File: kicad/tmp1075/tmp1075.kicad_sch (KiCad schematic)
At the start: 17 parts, among them J1 Conn_01x05, J2 Conn_01x05, U1 TMP1075DSG

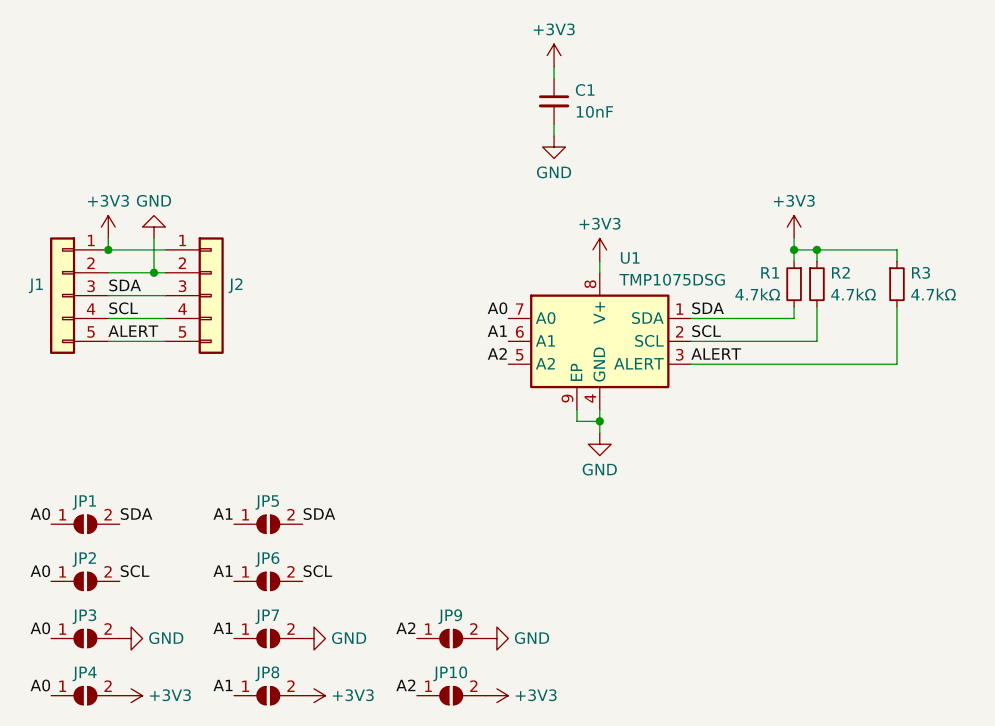
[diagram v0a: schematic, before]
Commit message: take 2 on tmp1075 breakout
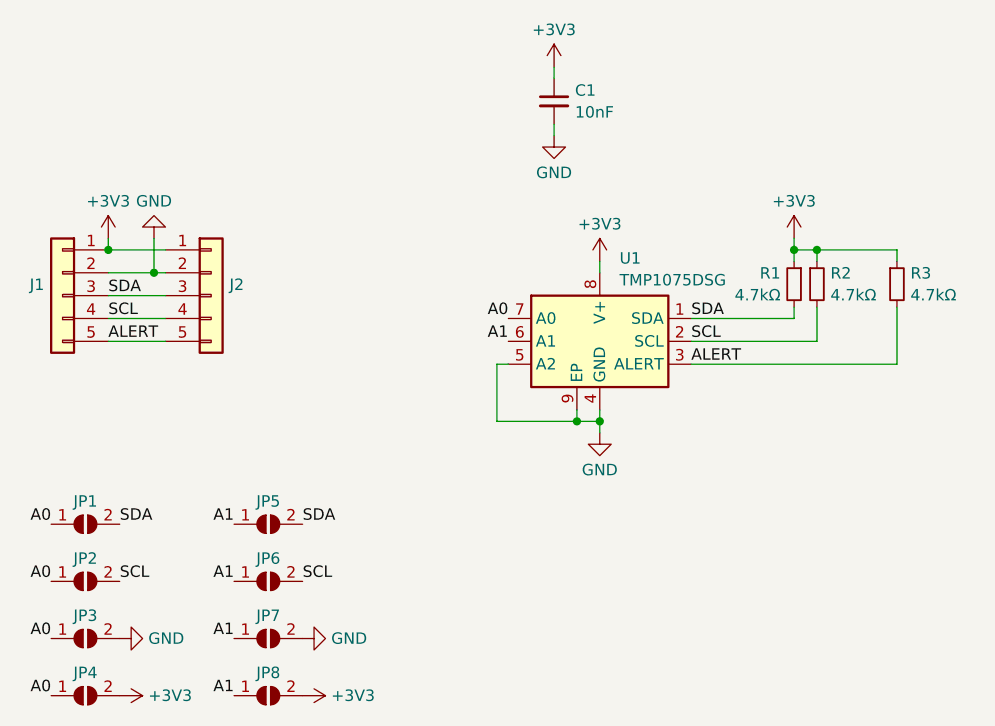
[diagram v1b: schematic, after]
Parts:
- removed JP10, JP9: SolderJumper_2_Open, Resistor_SMD:R_0201_0603Metric, symbol Jumper:SolderJumper_2_Open
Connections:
- net A2 is gone; now on net GND: U1.5 (A2)
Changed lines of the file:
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@@
   (junction (at 62.23 73.66) (diameter 0) (color 0 0 0 0)
   )
+  (junction (at 109.22 90.17) (diameter 0) (color 0 0 0 0)
+  )
   (wire (pts (xy 121.92 83.82) (xy 144.78 83.82))
     (stroke (width 0) (type default))
@@
     (stroke (width 0) (type default))
   )
+  (wire (pts (xy 101.6 83.82) (xy 100.33 83.82))
+    (stroke (width 0) (type default))
+  )
   (wire (pts (xy 133.35 69.85) (xy 133.35 71.12))
     (stroke (width 0) (type default))
@@
     (stroke (width 0) (type default))
   )
+  (wire (pts (xy 100.33 90.17) (xy 109.22 90.17))
+    (stroke (width 0) (type default))
+  )
   (wire (pts (xy 135.89 71.12) (xy 135.89 72.39))
     (stroke (width 0) (type default))
@@
     (stroke (width 0) (type default))
   )
+  (wire (pts (xy 100.33 83.82) (xy 100.33 90.17))
+    (stroke (width 0) (type default))
+  )
   (wire (pts (xy 133.35 71.12) (xy 133.35 72.39))
     (stroke (width 0) (type default))
   )
-  (label "A2" (at 91.44 114.3 180) (fields_autoplaced)
-    (effects (font (size 1.27 1.27)) (justify right bottom))
-  )
   (label "ALERT" (at 121.92 83.82 0) (fields_autoplaced)
     (effects (font (size 1.27 1.27)) (justify left bottom))
@@
     (effects (font (size 1.27 1.27)) (justify left bottom))
   )
-  (label "A2" (at 91.44 120.65 180) (fields_autoplaced)
-    (effects (font (size 1.27 1.27)) (justify right bottom))
-  )
   (label "A0" (at 101.6 78.74 180) (fields_autoplaced)
     (effects (font (size 1.27 1.27)) (justify right bottom))
@@
   )
   (label "A1" (at 101.6 81.28 180) (fields_autoplaced)
-    (effects (font (size 1.27 1.27)) (justify right bottom))
-  )
-  (label "A2" (at 101.6 83.82 180) (fields_autoplaced)
     (effects (font (size 1.27 1.27)) (justify right bottom))
   )
@@
     )
   )
-  (symbol (lib_id "Jumper:SolderJumper_2_Open") (at 95.25 114.3 0) (unit 1)
-    (in_bom yes) (on_board yes) (dnp no)
-    (property "Reference" "JP9" (at 95.25 111.76 0)
-      (effects (font (size 1.27 1.27)))
-    )
-    (property "Value" "SolderJumper_2_Open" (at 95.25 111.6909 0)
-      (effects (font (size 1.27 1.27)) hide)
-    )
-    (property "Footprint" "Resistor_SMD:R_0201_0603Metric" (at 95.25 114.3 0)
-      (effects (font (size 1.27 1.27)) hide)
-    )
-    (property "Datasheet" "~" (at 95.25 114.3 0)
-      (effects (font (size 1.27 1.27)) hide)
-    )
-    (pin "1")
-    (pin "2")
-    (instances
-      (project "tmp1075"
-        (path "/9963f092-e7ef-465f-bbaa-77706586bf9a"
-          (reference "JP9") (unit 1)
-        )
-      )
-    )
-  )
   (symbol (lib_id "power:GND") (at 111.76 91.44 0) (unit 1)
     (in_bom yes) (on_board yes) (dnp no) (fields_autoplaced)
@@
     )
   )
-  (symbol (lib_id "Jumper:SolderJumper_2_Open") (at 95.25 120.65 0) (unit 1)
-    (in_bom yes) (on_board yes) (dnp no)
-    (property "Reference" "JP10" (at 95.25 118.11 0)
-      (effects (font (size 1.27 1.27)))
-    )
-    (property "Value" "SolderJumper_2_Open" (at 95.25 118.0409 0)
-      (effects (font (size 1.27 1.27)) hide)
-    )
-    (property "Footprint" "Resistor_SMD:R_0201_0603Metric" (at 95.25 120.65 0)
-      (effects (font (size 1.27 1.27)) hide)
-    )
-    (property "Datasheet" "~" (at 95.25 120.65 0)
-      (effects (font (size 1.27 1.27)) hide)
-    )
-    (pin "1")
-    (pin "2")
-    (instances
-      (project "tmp1075"
-        (path "/9963f092-e7ef-465f-bbaa-77706586bf9a"
-          (reference "JP10") (unit 1)
-        )
-      )
-    )
-  )
   (symbol (lib_id "Device:R_Small") (at 135.89 74.93 0) (unit 1)
     (in_bom yes) (on_board yes) (dnp no) (fields_autoplaced)
@@
         (path "/9963f092-e7ef-465f-bbaa-77706586bf9a"
           (reference "R2") (unit 1)
-        )
-      )
-    )
-  )
-  (symbol (lib_id "power:+3V3") (at 99.06 120.65 270) (unit 1)
-    (in_bom yes) (on_board yes) (dnp no) (fields_autoplaced)
-    (property "Reference" "#PWR011" (at 95.25 120.65 0)
-      (effects (font (size 1.27 1.27)) hide)
-    )
-    (property "Value" "+3V3" (at 102.235 120.65 90)
-      (effects (font (size 1.27 1.27)) (justify left))
-    )
-    (property "Footprint" "" (at 99.06 120.65 0)
-      (effects (font (size 1.27 1.27)) hide)
-    )
-    (property "Datasheet" "" (at 99.06 120.65 0)
-      (effects (font (size 1.27 1.27)) hide)
-    )
-    (pin "1")
-    (instances
-      (project "tmp1075"
-        (path "/9963f092-e7ef-465f-bbaa-77706586bf9a"
-          (reference "#PWR011") (unit 1)
         )
       )
@@
         )
       )
-    )
-  )
-  (symbol (lib_id "power:GND") (at 99.06 114.3 90) (unit 1)
-    (in_bom yes) (on_board yes) (dnp no) (fields_autoplaced)
-    (property "Reference" "#PWR010" (at 105.41 114.3 0)
-      (effects (font (size 1.27 1.27)) hide)
-    )
-    (property "Value" "GND" (at 102.235 114.3 90)
-      (effects (font (size 1.27 1.27)) (justify right))
-    )
-    (property "Footprint" "" (at 99.06 114.3 0)
-      (effects (font (size 1.27 1.27)) hide)
-    )
-    (property "Datasheet" "" (at 99.06 114.3 0)
-      (effects (font (size 1.27 1.27)) hide)
-    )
-    (pin "1")
-    (instances
-      (project "tmp1075"
-        (path "/9963f092-e7ef-465f-bbaa-77706586bf9a"
-          (reference "#PWR010") (unit 1)
-        )
-      )
